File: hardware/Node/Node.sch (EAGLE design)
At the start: 41 parts, among them SW1 KSS, SW2 KSS, U1 ATMEGA32U4QFN, U2 BLUETOOTH-RN41", U3 LSM303DLM, U4 L3GD20, U5 8.0MHz, U6 MCP73831, U7 V_REG_LDOSMD, X1 USBSMD

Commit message: Complete alpha revision schematic
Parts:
- removed LED2, LED3: (no value), SparkFun:LED0603
- added C14: 1uF, SparkFun:CAP0603-CAP
- added C15: 10nF, SparkFun:CAP0603-CAP
- added C16, C17, C18, C19, C20: 100nF, SparkFun:CAP0603-CAP
- added HWB, RESET: KSS, adjacent-reality:KSS
- added J1: AVR_SPI_PRG_6NS, SparkFun:AVR_SPI_PRG_6NS
- added JP2: (no value), SparkFun:PINHD-2X3
- added POWER: (no value), SparkFun:SWITCH-SPST-SMD-A
- added R10: 1.0k, SparkFun:RESISTOR0603-RES
- added R11: 150, SparkFun:RESISTOR0603-RES
- added U8: MAX1704X, SparkFun:MAX1704X
- R2: value 470 -> 10k
- R4: value 220 -> 330
- renumbered U$1 to U9
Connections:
- removed net N$14 (its old number): LED3.C, R4.2
- new net HWB: HWB.3, U1.PE2/!HWB
- new net MISO: J1.1, U1.PB3(MISO)
- new net MOSI: J1.4, U1.PB2(MOSI)
- new net N$16: JP1.1, POWER.S
- new net N$29: C14.1, R10.1, U8.CELL
- new net N$30: C15.1, R11.1, U8.VDD
- new net N$31: JP2.3, U1.PF6(ADC6)
- new net N$32: JP2.5, U1.PF5(ADC5)
- new net N$33: JP2.2, U1.PF4(ADC4)
- new net N$34: JP2.4, U1.PF1(ADC1)
- new net N$35: JP2.6, U1.PF0(ADC0)
- new net PCINT7: U1.PB7, U8.ALT
- new net RBT: U1.PD4(ADC8), U2.RESET
- new net RESET: J1.5, R4.1, RESET.3
- new net SBT: U1.PE6, U2.PIO2
- new net SCK: J1.3, U1.PB1(SCK)
- net +3V3: now also C16.1, C17.1, C18.1, C19.1, J1.2, R2.2; no longer U2.RESET
- net GND: now also C14.2, C15.2, C16.2, C17.2, C18.2, C19.2, C20.2, HWB.1, J1.6, RESET.1, U8.CTG, U8.GND@4, U8.GND@EP, U8.QST; no longer LED1.C, R4.1
- net N$10: now also LED4.RED-C, R5.2; no longer LED1.A, R2.1
- net N$11: now also POWER.P, R10.2, R11.2; no longer JP1.1
- net N$12: now also LED1.C; no longer LED2.C
- net N$13: now also SW1.1, U1.PB0(SS); no longer LED3.A, U2.PIO5
- net N$18: now also R5.1; no longer R5.2
- net N$19: now also SW2.1, U1.PD5; no longer LED4.RED-C, R5.1
- net N$27: now also C20.1, R2.1, R4.2, U1.!RESET; no longer SW2.1, U1.PF0(ADC0)
- net N$28: now also JP2.1, U1.PF7(ADC7); no longer SW1.1, U1.PF1(ADC1)
- net N$4: no longer R2.2
- net SCL: now also U8.SCL
- net SDA: now also U8.SDA
- net VBUS: now also LED1.A; no longer LED2.A
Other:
- moved on the sheet: C10, C11, C12, C13, C8, C9, JP1, LED1, LED4, R1, R2, R3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

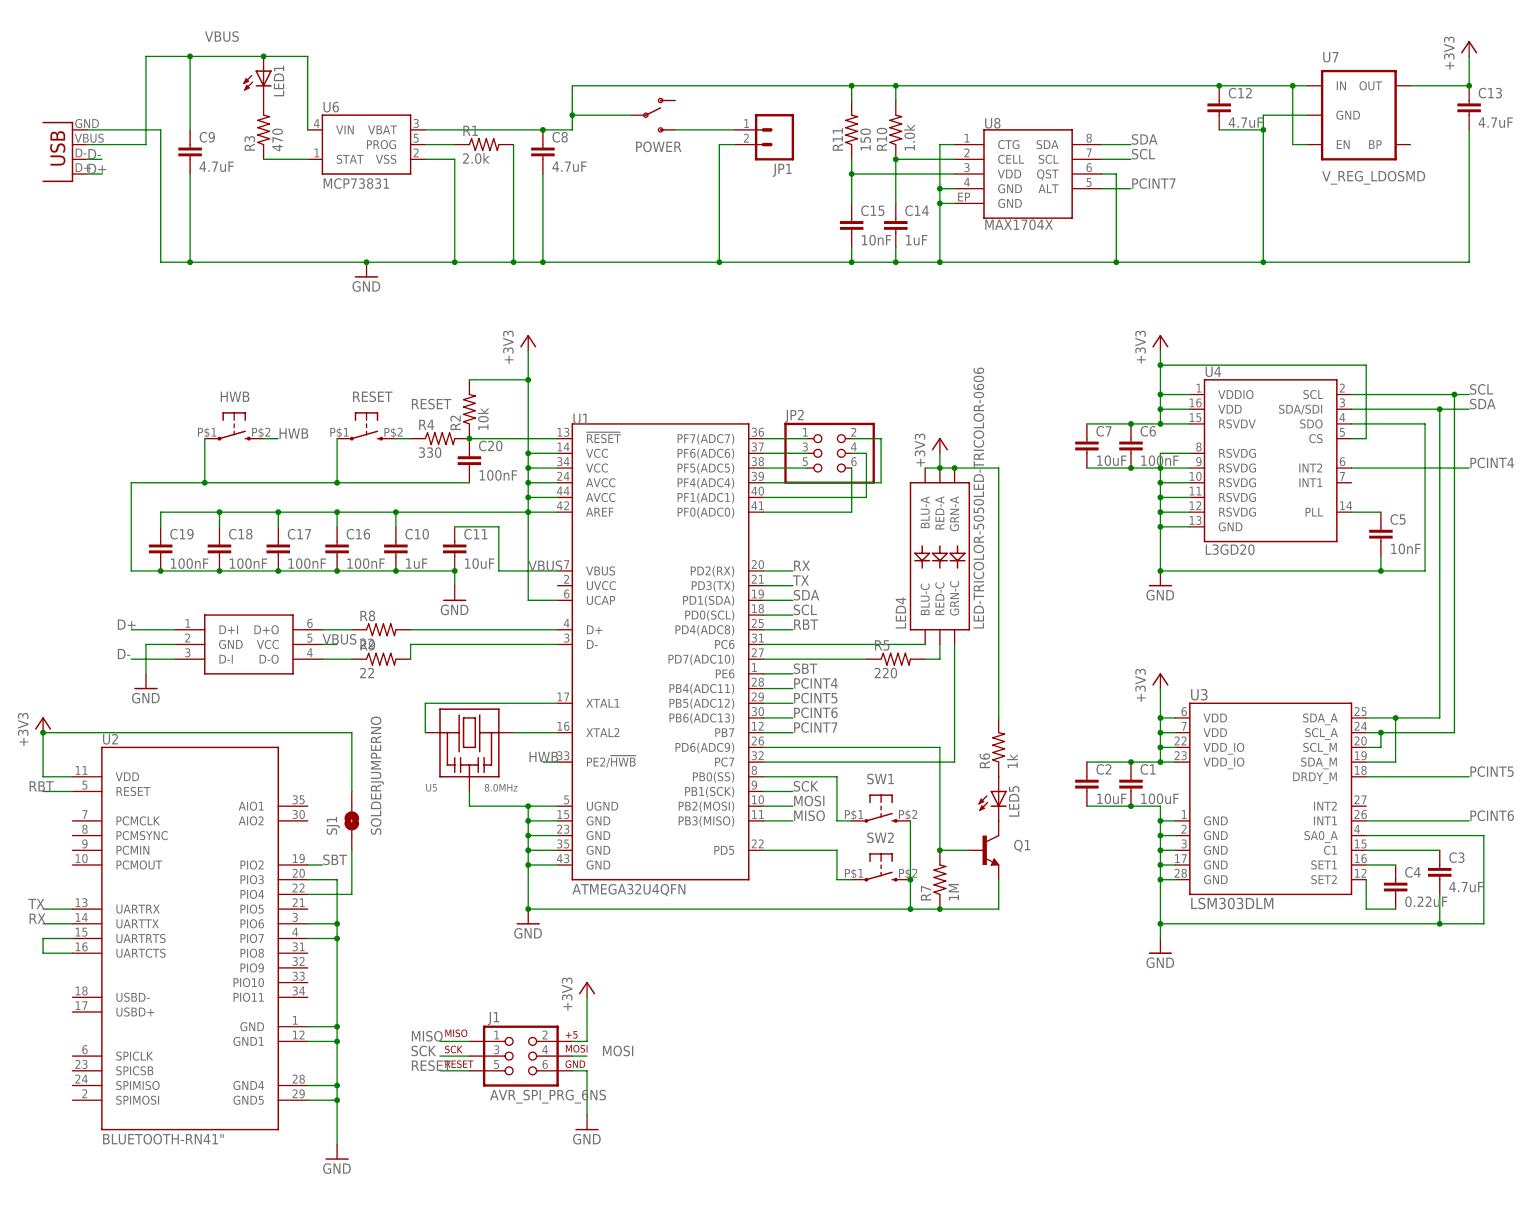
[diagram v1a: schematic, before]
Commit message: Added nfet style level shift Moved switch to other side of MAX1704x Changed C1 value from 100uF to 100nF Changed U1 symbol from NPN to NFET Added optional pullups on SDA/SCL Pullup on HWB Changed resistor/ capactior packages Generic names/values Pinswapped TVS array D+/D- for layout ease Added test points on interrupt lines
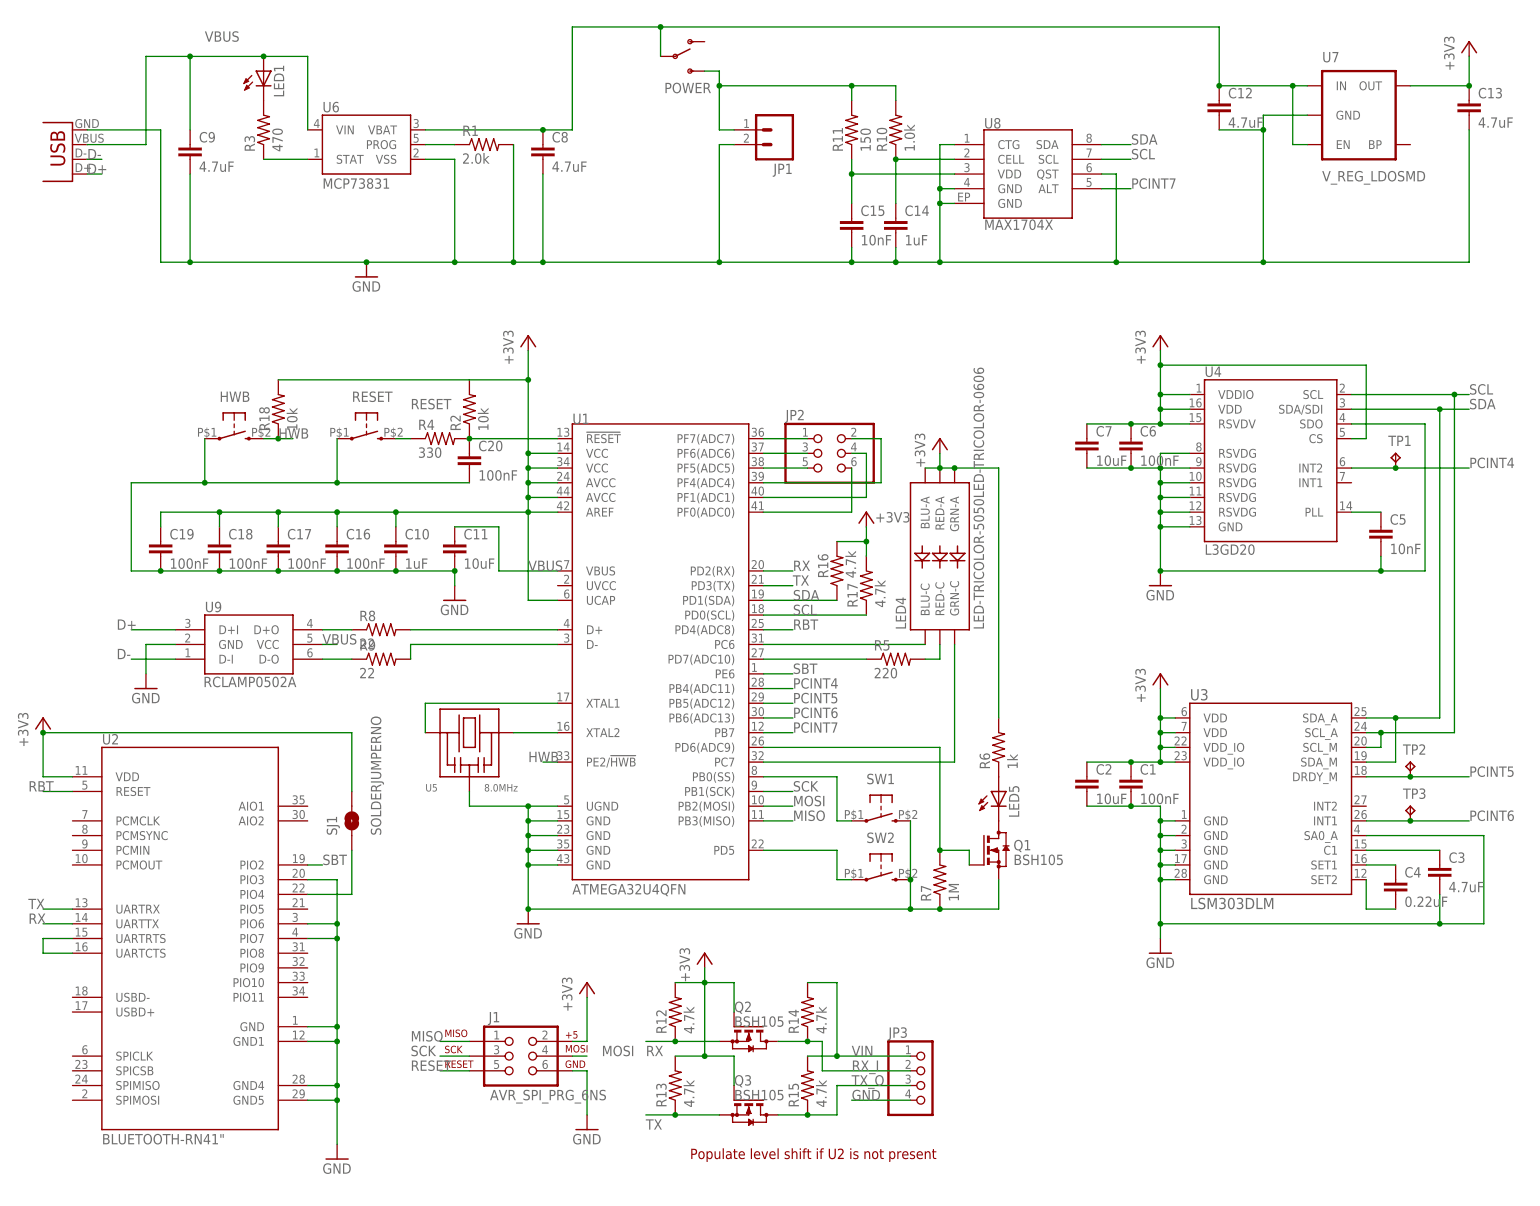
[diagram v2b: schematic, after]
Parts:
- added JP3: (no value), pinhead:PINHD-1X4
- added Q2, Q3: BSH105, transistor-small-signal:BSS123
- added R12, R13, R14, R15, R16, R17: 4.7k, SparkFun:RESISTOR0402-RES
- added R18: 10k, SparkFun:RESISTOR0402-RES
- added TP1, TP2, TP3: TPTP06R, testpad:TPTP06R
- C1: value 100uF -> 100nF; device SparkFun:CAP0603-CAP -> SparkFun:CAP0402-CAP
- C10, C14, C15, C16, C17, C18, C19, C4, C5, C6: device SparkFun:CAP0603-CAP -> SparkFun:CAP0402-CAP
- Q1: value (none) -> BSH105; device SparkFun:TRANSISTOR_NPNSOT23 -> transistor-small-signal:BSS123
- R1, R10, R11, R2, R3, R4, R5, R6, R7, R8, R9: device SparkFun:RESISTOR0603-RES -> SparkFun:RESISTOR0402-RES
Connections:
- removed net N$16: JP1.1, POWER.S
- new net N$36: JP1.1, POWER.S, R10.2, R11.2
- new net RX_I: JP3.2, Q2.D, R14.1
- new net TX_O: JP3.3, Q3.D, R15.1
- new net VIN: JP3.1, R14.2, R15.2
- net +3V3: now also Q2.G, Q3.G, R12.2, R13.2, R16.2, R17.2, R18.2
- net GND: now also JP3.4, Q1.S; no longer Q1.E
- net HWB: now also R18.1
- net N$11: no longer R10.2, R11.2
- net N$20: now also Q1.D; no longer Q1.C
- net N$22: now also Q1.G; no longer Q1.B
- net PCINT4: now also TP1.TP
- net PCINT5: now also TP2.TP
- net PCINT6: now also TP3.TP
- net RX: now also Q2.S, R12.1
- net SCL: now also R17.1
- net SDA: now also R16.1
- net TX: now also Q3.S, R13.1
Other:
- note added: "Populate level shift if U2 is not present"
- moved on the sheet: POWER

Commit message: use mcp73871 and cleanup
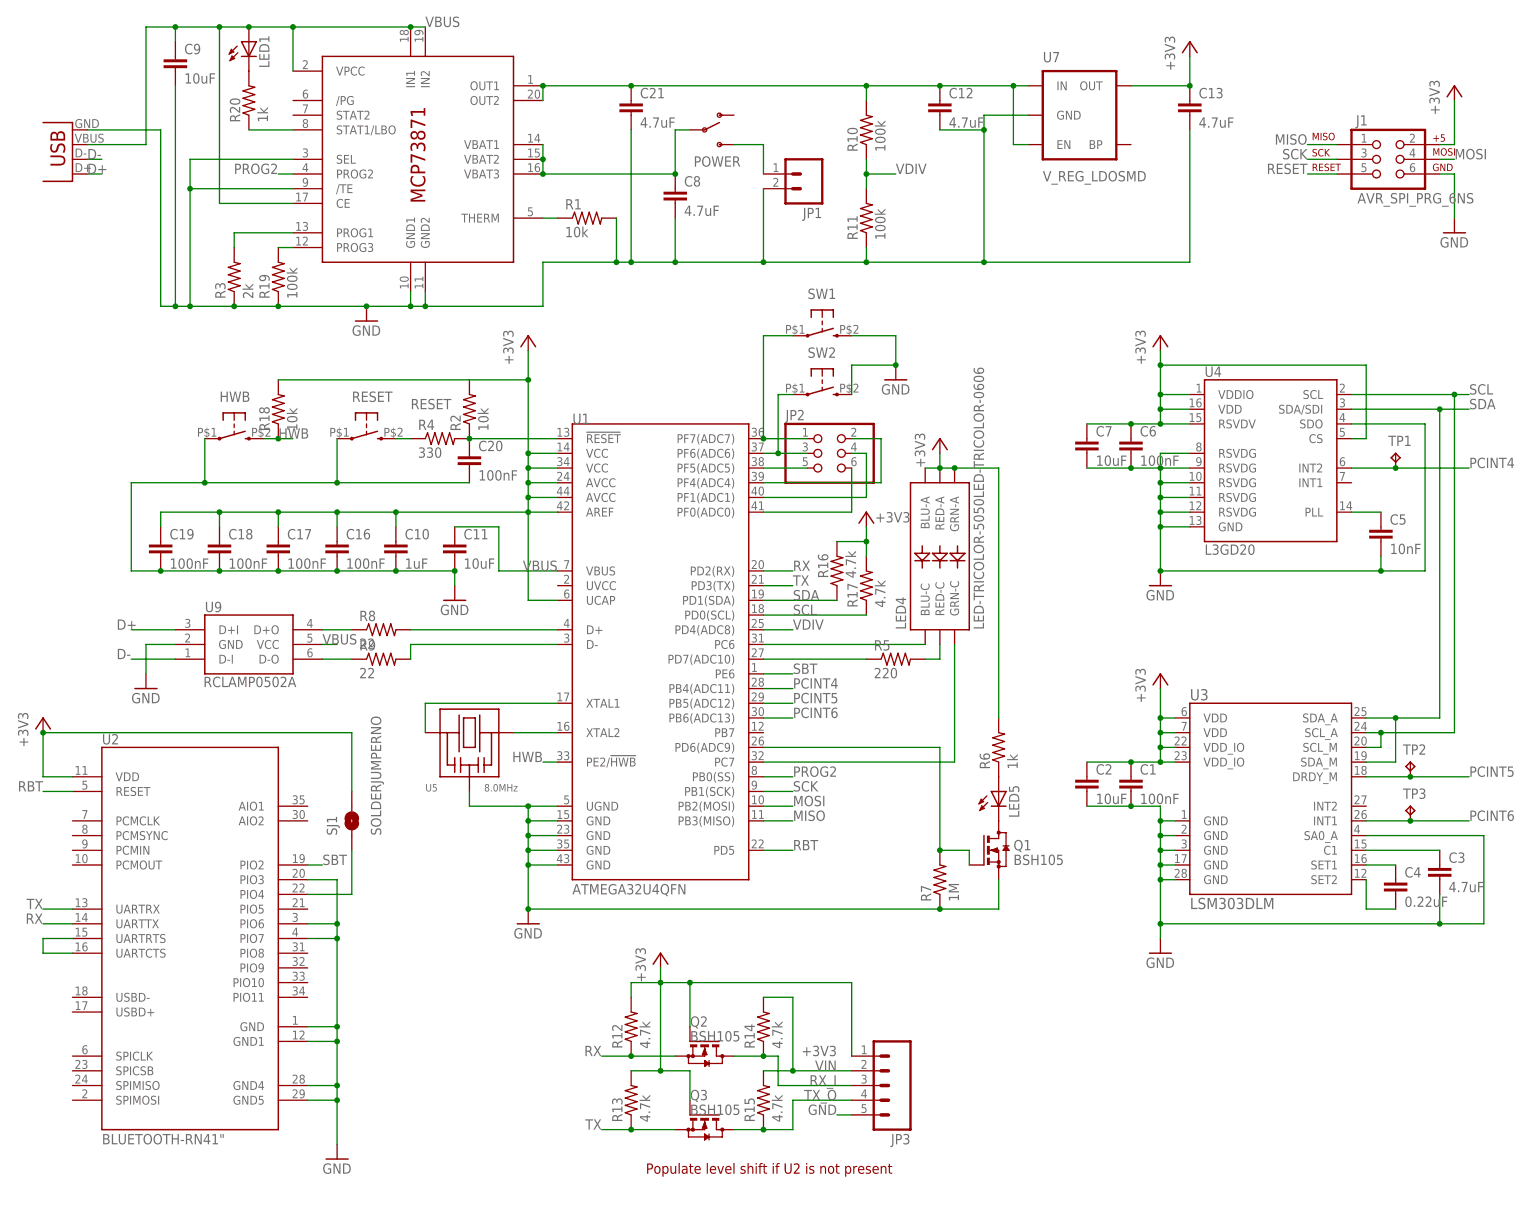
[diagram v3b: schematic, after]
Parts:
- removed C14: 1uF, SparkFun:CAP0402-CAP
- removed C15: 10nF, SparkFun:CAP0402-CAP
- removed U8: MAX1704X, SparkFun:MAX1704X
- added C21: 4.7uF, SparkFun:CAP0402-CAP
- added R19: 100k, SparkFun:RESISTOR0402-RES
- added R20: 1k, SparkFun:RESISTOR0402-RES
- C8: device SparkFun:CAP0603-CAP -> SparkFun:CAP0402-CAP
- C9: value 4.7uF -> 10uF
- JP3: device pinhead:PINHD-1X4 -> SparkFun:M05PTH
- R1: value 2.0k -> 10k
- R10: value 1.0k -> 100k
- R11: value 150 -> 100k
- R3: value 470 -> 2k
- U6: value MCP73831 -> MCP73871; device SparkFun:MCP73831 -> adafruit:MCP73871
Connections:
- removed net N$12: LED1.C, R3.2
- removed net N$30: C15.1, R11.1, U8.VDD
- removed net PCINT7: U1.PB7, U8.ALT
- new net N$16: R3.2, U6.PROG1
- new net PROG2: U1.PB0(SS), U6.PROG2
- new net VDIV: R10.1, R11.2, U1.PD4(ADC8)
- net +3V3: now also JP3.1
- net GND: now also C21.2, JP3.5, R11.1, R19.1, R3.1, U6./TE, U6.GND1, U6.GND2, U6.SEL; no longer C14.2, C15.2, JP3.4, U6.VSS, U8.CTG, U8.GND@4, U8.GND@EP, U8.QST
- net N$11: now also C21.1, R10.2, U6.OUT1, U6.OUT2; no longer C8.1, POWER.P, U6.VBAT
- net N$13: now also LED1.C, R20.2; no longer SW1.1, U1.PB0(SS)
- net N$19: now also R20.1, U6.STAT1/LBO; no longer SW2.1, U1.PD5
- net N$28: now also SW1.1
- net N$29: now also JP1.1, POWER.S; no longer C14.1, R10.1, U8.CELL
- net N$31: now also SW2.1
- net N$36: now also R19.2, U6.PROG3; no longer JP1.1, POWER.S, R10.2, R11.2
- net N$4: now also C8.1, POWER.P, U6.VBAT1, U6.VBAT2, U6.VBAT3; no longer R3.1, U6.STAT
- net N$8: now also U6.THERM; no longer U6.PROG
- net RBT: now also U1.PD5; no longer U1.PD4(ADC8)
- net RX_I: now also JP3.3; no longer JP3.2
- net SCL: no longer U8.SCL
- net SDA: no longer U8.SDA
- net TX_O: now also JP3.4; no longer JP3.3
- net VBUS: now also U6.CE, U6.IN1, U6.IN2, U6.VPCC; no longer U6.VIN
- net VIN: now also JP3.2; no longer JP3.1
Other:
- moved on the sheet: C12, C13, C8, C9, J1, JP1, LED1, POWER, Q2, Q3, R1, R10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

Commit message: switched mosfets
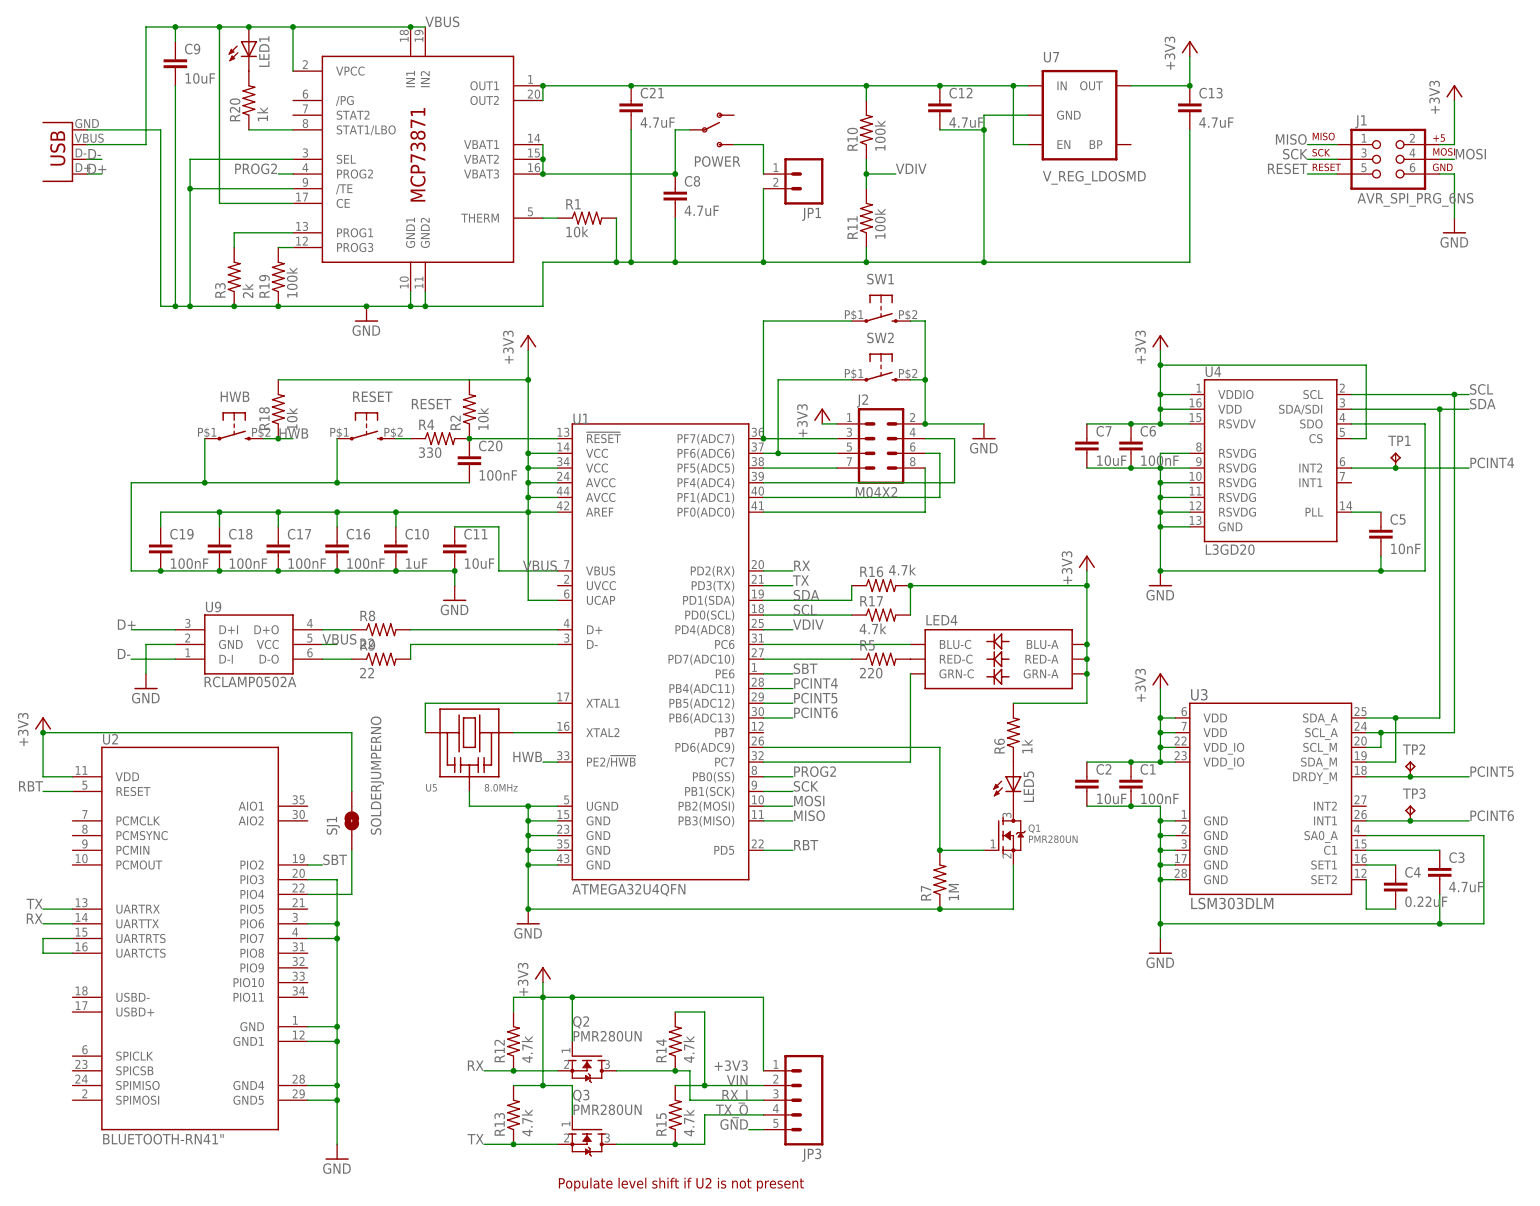
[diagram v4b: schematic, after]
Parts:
- removed JP2: (no value), SparkFun:PINHD-2X3
- added J2: M04X2, SparkFun:M04X2
- C20: device SparkFun:CAP0603-CAP -> SparkFun:CAP0402-CAP
- C21, C8: device SparkFun:CAP0402-CAP -> SparkFun:CAP0603-CAP
- Q1, Q2, Q3: value BSH105 -> PMR280UN; device transistor-small-signal:BSS123 -> adjacent-reality:MOSFET-N
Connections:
- net +3V3: now also J2.1
- net GND: now also J2.2
- net N$28: now also J2.3; no longer JP2.1
- net N$31: now also J2.5; no longer JP2.3
- net N$32: now also J2.7; no longer JP2.5
- net N$33: now also J2.4; no longer JP2.2
- net N$34: now also J2.6; no longer JP2.4
- net N$35: now also J2.8; no longer JP2.6
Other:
- moved on the sheet: JP3, LED4, LED5, R12, R13, R14, R15, R16, R17, R5, R6, SW1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
